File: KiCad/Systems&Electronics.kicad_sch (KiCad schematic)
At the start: 42 parts, among them U13 AD8495, U14 AD8495, U15 AD8495, U16 AD8495, U3 MAX485E, U4 MAX485E

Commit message: fixed the 4th solenoid
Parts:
- removed D2: LED, symbol Device:LED
- removed R5: 220, symbol Device:R
- added 5V Relay5: ~, symbol 5VRelay:5V_Relay
- added Solenoid4: ~, symbol Solenoids:Solenoid
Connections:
- net +12V: now also 5V Relay5. (NO)
- net at R3.1, U3.3 (DE), U3.4 (DI): now also U3.2 (~{RE})
- net at Solenoid1. (-): now also 5V Relay4. (NO), D2.2 (A), D3.1 (K), Solenoid2. (-), Solenoid3. (-), Solenoid4. (-); no longer 5V Relay1. (NO)
- net at Pressure_Transducer1. (VCC), Pressure_Transducer2. (VCC), Pressure_Transducer3. (VCC)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: now also A1.GND1 (GND); no longer A1.5V3 (5V)
- net at A1.D29: now also 5V Relay5. (NO)
- net at R2.1, U4.2 (~{RE}): now also U4.1 (RO)
- new net: 5V Relay1. (NO), 5V Relay2. (NO), 5V Relay3. (NO), 5V Relay4. (NO), 5V Relay5. (NO), A1.5V4 (5V), A1.GND5 (GND)
- new net: 5V Relay5. (NO), Solenoid4. (-)
- new net: 5V Relay1. (NO), Solenoid1. (-)
- new net: A1.5V3 (5V), Pressure_Transducer1. (VCC), Pressure_Transducer2. (VCC), Pressure_Transducer3. (VCC), Pressure_Transducer4. (VCC), Pressure_Transducer5. (VCC), Pressure_Transducer6. (VCC)
- new net: HX711_Board1. (VCC), Load_Cell1. (VCC) (x3)
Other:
- moved on the sheet: 5V Relay1, 5V Relay2, 5V Relay3, 5V Relay4, D3, HX711_Board1, Load_Cell1, Solenoid1, Solenoid2, Solenoid3

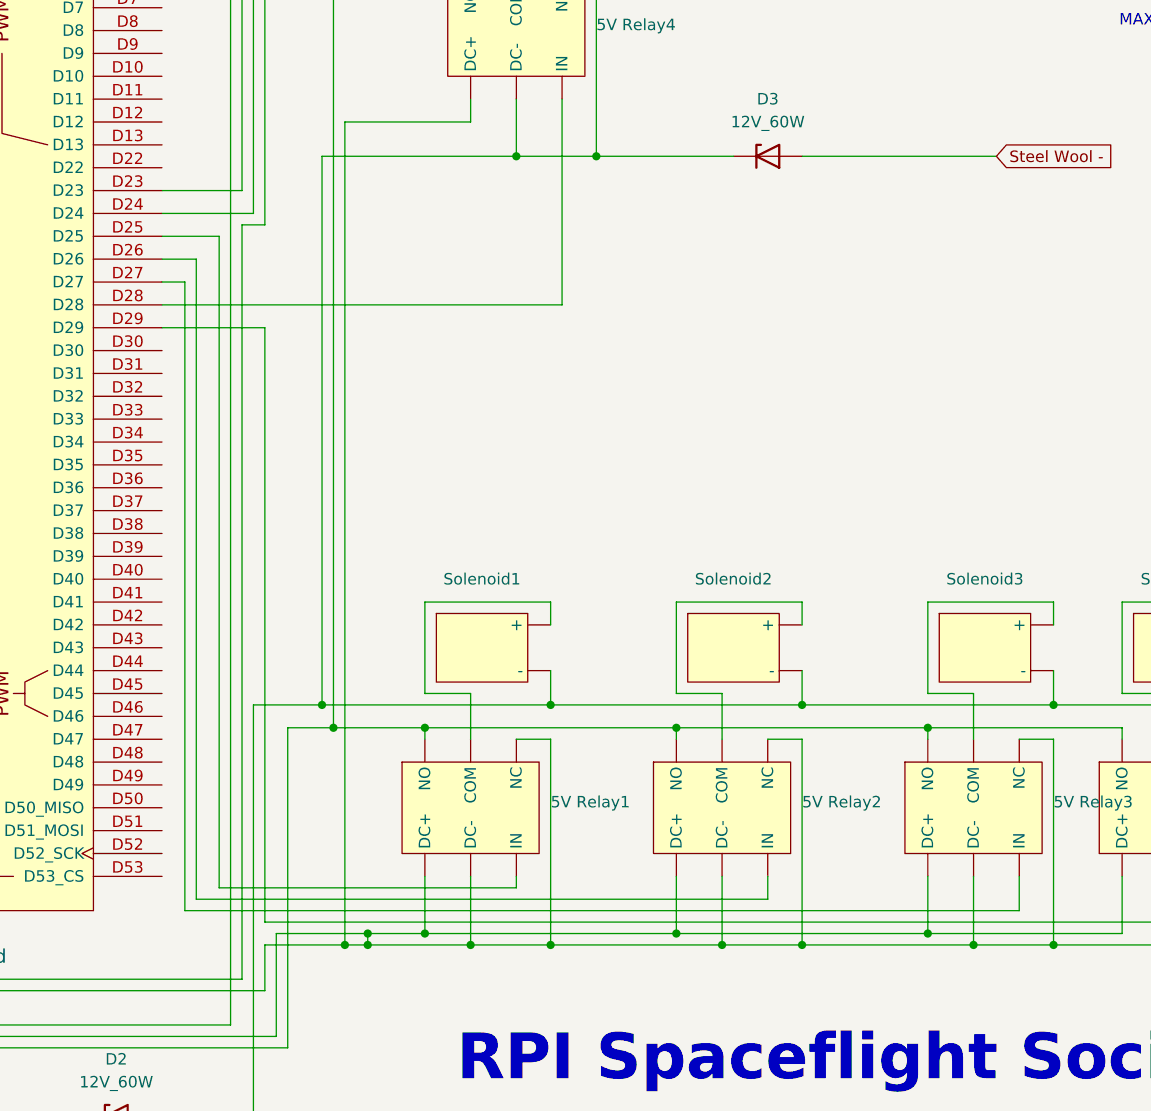
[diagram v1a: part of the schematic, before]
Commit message: add Leds
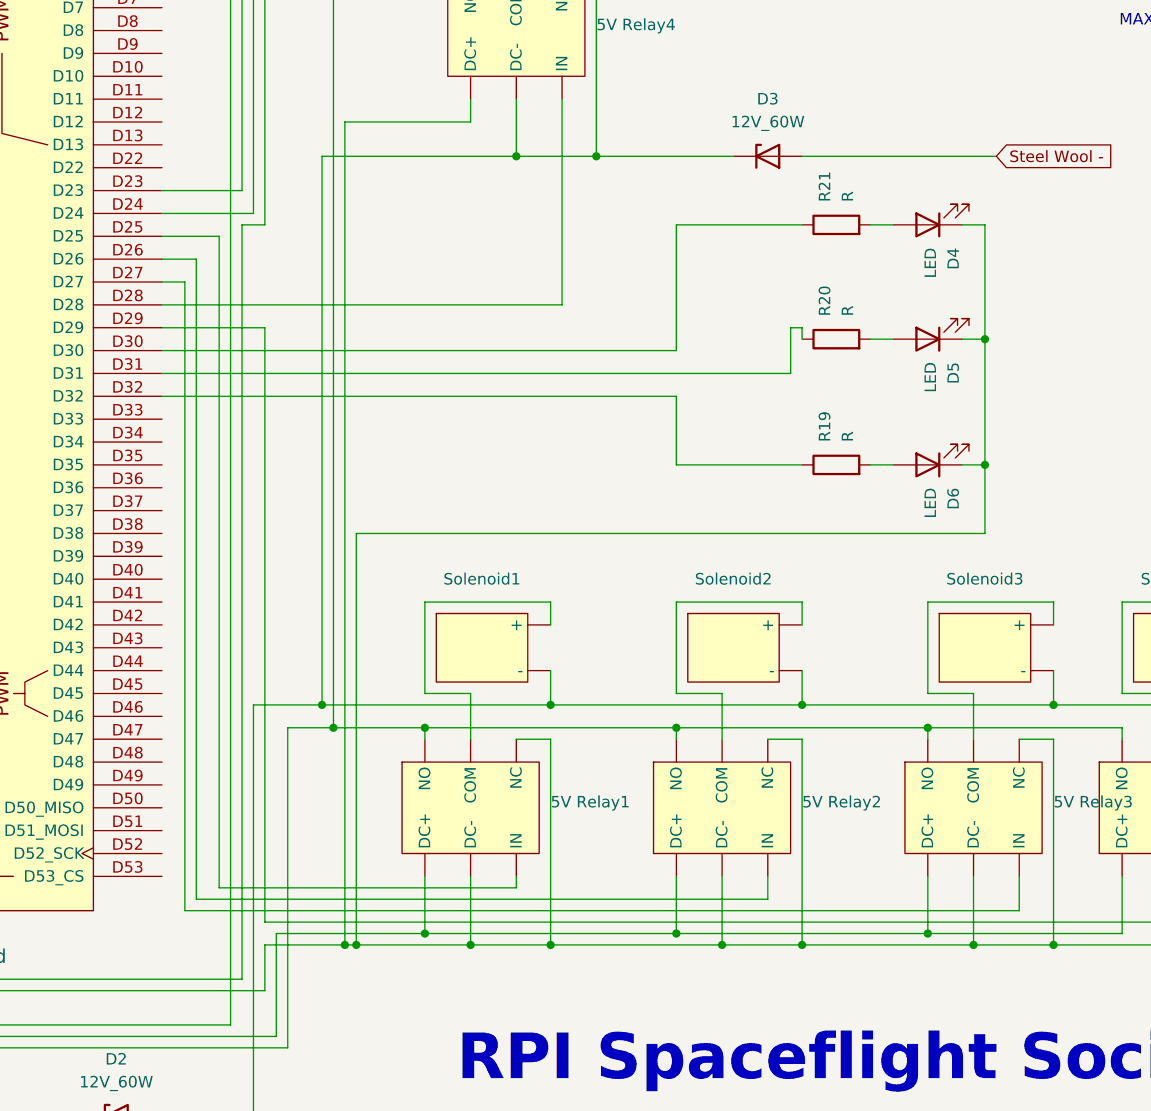
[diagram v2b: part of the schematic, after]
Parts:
- added D4, D5, D6: LED, symbol Device:LED
- added R19, R20, R21: R, symbol Device:R
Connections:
- net at Solenoid4. (-): now also 5V Relay4. (NO), D2.2 (A), D3.1 (K), Solenoid1. (-), Solenoid2. (-), Solenoid3. (-); no longer 5V Relay5. (NO)
- net at Pressure_Transducer1. (VCC), Pressure_Transducer2. (VCC), Pressure_Transducer3. (VCC)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: now also A1.GND1 (GND); no longer A1.5V3 (5V)
- net at A1.D30: now also R21.1
- net at A1.D31: now also R20.1
- net at A1.D32: now also R19.1
- new net: 5V Relay1. (NO), 5V Relay2. (NO), 5V Relay3. (NO), 5V Relay4. (NO), 5V Relay5. (NO), A1.GND5 (GND), D4.1 (K), D5.1 (K), D6.1 (K)
- new net: 5V Relay1. (NO), 5V Relay2. (NO), 5V Relay3. (NO), 5V Relay5. (NO), A1.5V4 (5V)
- new net: 5V Relay5. (NO), Solenoid4. (-)
- new net: 5V Relay1. (NO), Solenoid1. (-)
- new net: D4.2 (A), R21.2
- new net: A1.5V3 (5V), Pressure_Transducer1. (VCC), Pressure_Transducer2. (VCC), Pressure_Transducer3. (VCC), Pressure_Transducer4. (VCC), Pressure_Transducer5. (VCC), Pressure_Transducer6. (VCC)
- new net: D5.2 (A), R20.2
- new net: HX711_Board1. (VCC), Load_Cell1. (VCC) (x3)
- new net: D6.2 (A), R19.2

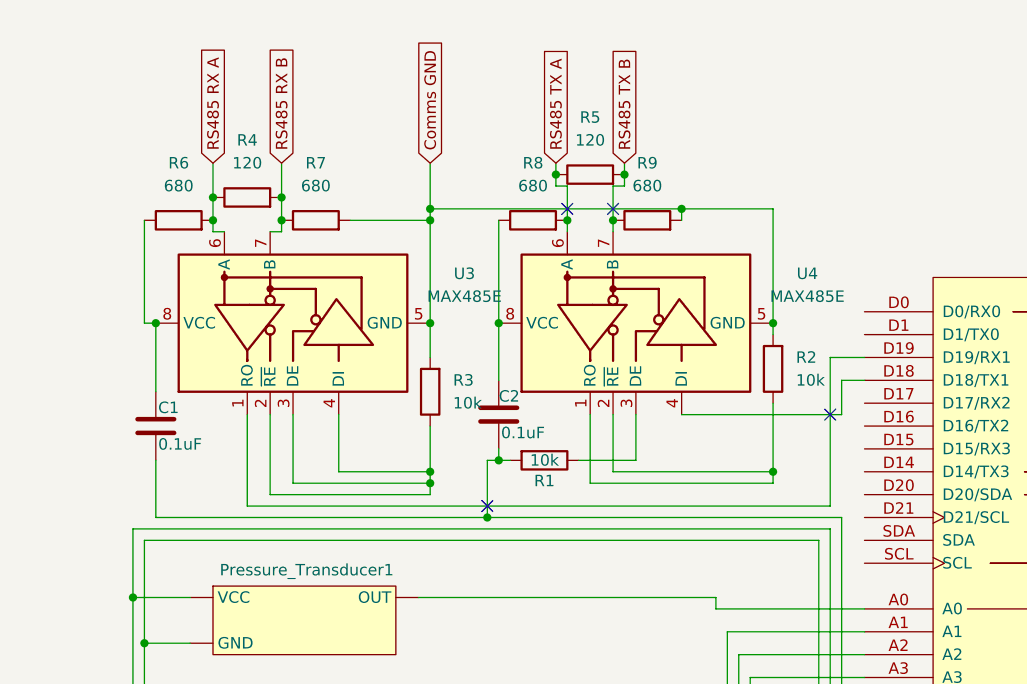
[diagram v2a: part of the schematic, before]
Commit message: Update Schematic to remove unneeded caps and resistors
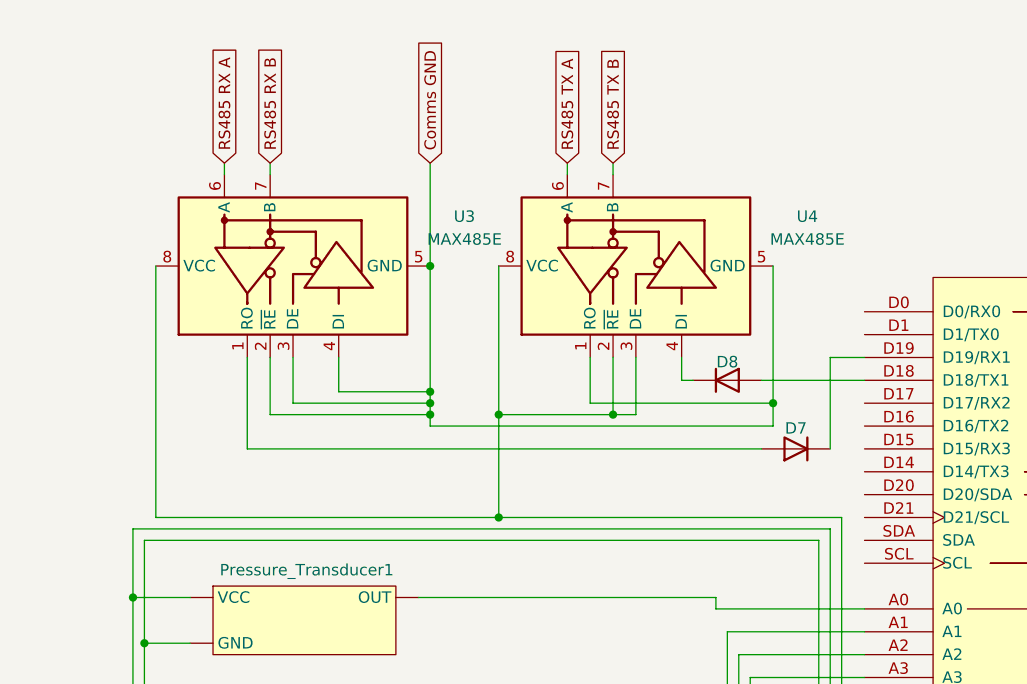
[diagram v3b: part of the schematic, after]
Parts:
- removed C1, C2: 0.1uF, symbol Device:C
- removed R1, R2, R3: 10k, symbol Device:R
- removed R4, R5: 120, symbol Device:R
- removed R6, R7, R8, R9: 680, symbol Device:R
- added D7, D8: D, symbol Device:D
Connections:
- net Comms GND: now also U3.2 (~{RE}), U3.3 (DE), U3.4 (DI), U4.1 (RO)
- net at Solenoid4. (-): now also 5V Relay4. (NO), D2.2 (A), D3.1 (K), Solenoid1. (-), Solenoid2. (-), Solenoid3. (-); no longer 5V Relay5. (NO)
- net at U3.8 (VCC): now also A1.5V1 (5V), U13.7 (+Vs), U14.7 (+Vs), U15.7 (+Vs), U16.7 (+Vs), U4.2 (~{RE}), U4.3 (DE), U4.8 (VCC)
- net at Pressure_Transducer1. (VCC), Pressure_Transducer2. (VCC), Pressure_Transducer3. (VCC)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: now also A1.GND1 (GND); no longer A1.5V3 (5V)
- net at A1.D18 (D18/TX1): now also D8.2 (A); no longer U4.4 (DI)
- net at A1.D19 (D19/RX1): now also D7.1 (K); no longer U3.1 (RO)
- new net: 5V Relay1. (NO), 5V Relay2. (NO), 5V Relay3. (NO), 5V Relay4. (NO), 5V Relay5. (NO), A1.GND5 (GND), D4.1 (K), D5.1 (K), D6.1 (K)
- new net: 5V Relay1. (NO), 5V Relay2. (NO), 5V Relay3. (NO), 5V Relay5. (NO), A1.5V4 (5V)
- new net: 5V Relay5. (NO), Solenoid4. (-)
- new net: 5V Relay1. (NO), Solenoid1. (-)
- new net: A1.5V3 (5V), Pressure_Transducer1. (VCC), Pressure_Transducer2. (VCC), Pressure_Transducer3. (VCC), Pressure_Transducer4. (VCC), Pressure_Transducer5. (VCC), Pressure_Transducer6. (VCC)
- new net: HX711_Board1. (VCC), Load_Cell1. (VCC) (x3)
- new net: D7.2 (A), U3.1 (RO)
- new net: D8.1 (K), U4.4 (DI)
- no-connect marks 4 -> 0
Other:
- moved on the sheet: U3, U4
